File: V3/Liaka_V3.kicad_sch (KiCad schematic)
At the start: 6 parts

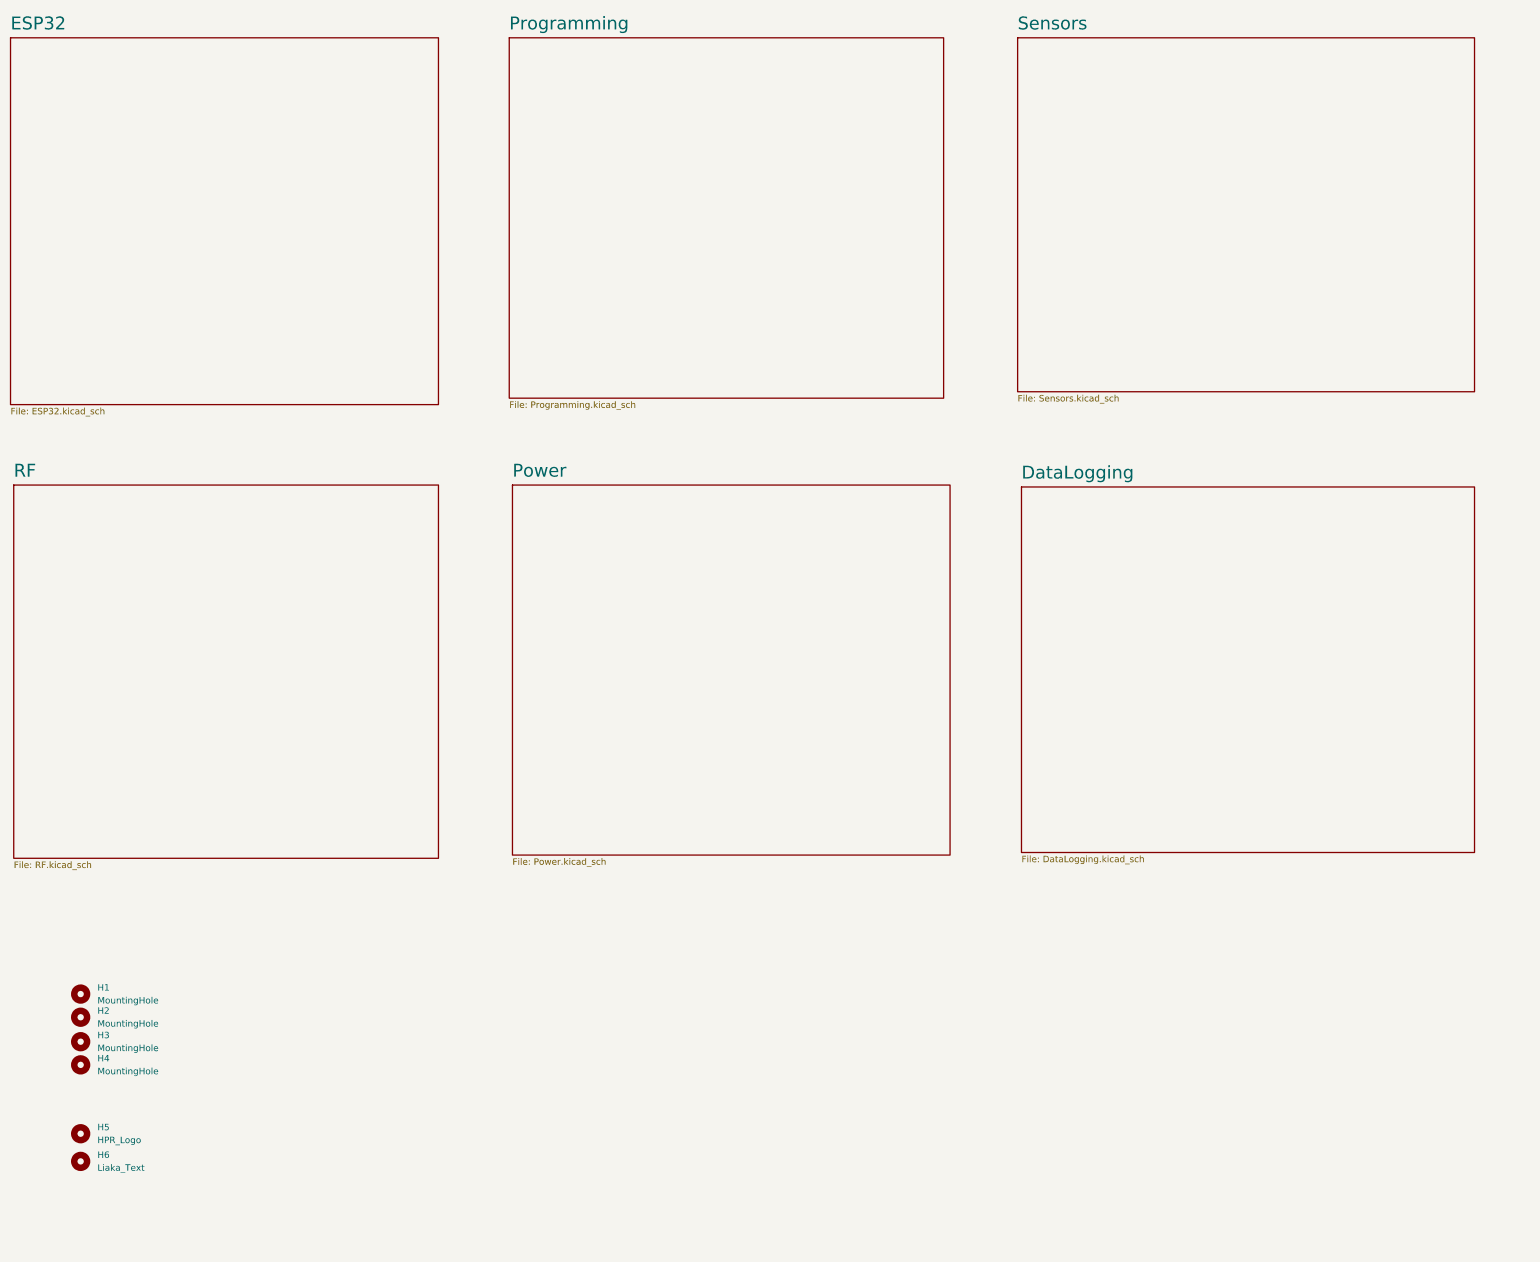
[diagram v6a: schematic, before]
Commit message: New parts placed and routed
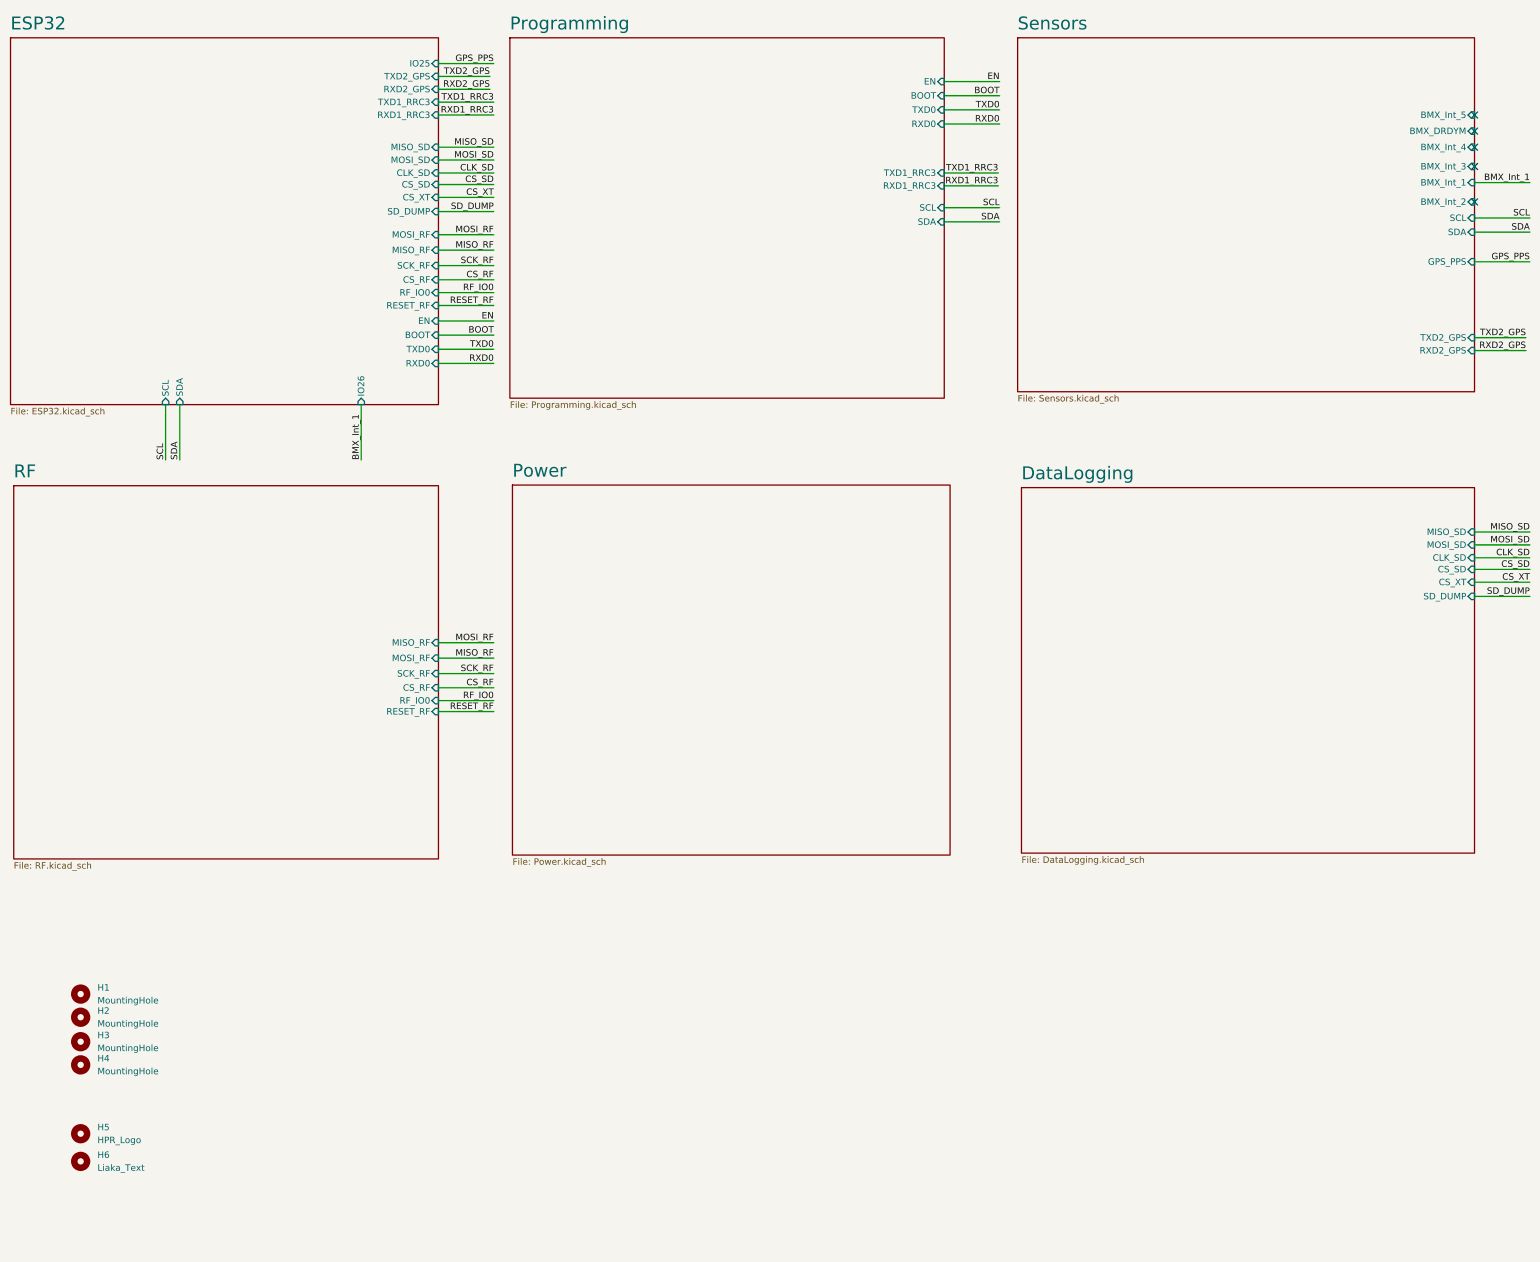
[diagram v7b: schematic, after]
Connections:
- no-connect marks 0 -> 5
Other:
- sheet DataLogging ports: added CLK_SD, CS_SD, CS_XT, MISO_SD, MOSI_SD, SD_DUMP; removed none
- sheet ESP32 ports: added BOOT, CLK_SD, CS_RF, CS_SD, CS_XT, EN, IO25, IO26, MISO_RF, MISO_SD, MOSI_RF, MOSI_SD, RESET_RF, RF_IO0, RXD0, RXD1_RRC3, RXD2_GPS, SCK_RF, SCL, SDA, SD_DUMP, TXD0, TXD1_RRC3, TXD2_GPS; removed none
- sheet Programming ports: added BOOT, EN, RXD0, RXD1_RRC3, SCL, SDA, TXD0, TXD1_RRC3; removed none
- sheet RF ports: added CS_RF, MISO_RF, MOSI_RF, RESET_RF, RF_IO0, SCK_RF; removed none
- sheet Sensors ports: added BMX_DRDYM, BMX_Int_1, BMX_Int_2, BMX_Int_3, BMX_Int_4, BMX_Int_5, GPS_PPS, RXD2_GPS, SCL, SDA, TXD2_GPS; removed none
